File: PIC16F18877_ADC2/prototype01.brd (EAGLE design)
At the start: 95 x 72 mm, 39 parts, among them CN1 12V_IN, CN10 PIC_PORTD_IF, CN2 PIC_PORTA_IF, CN3 UART_IF, CN4 PIC_CN_H, CN5 AE-MICRO-SD-DIP, CN6 I2C_IF, CN7 PIC_PORTB_IF, CN8 PIC_PORTE_IF, CN9 PIC_PORTC_IF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

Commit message: 実体配線図の初版
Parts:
- moved R2 10.3 mm to (72.4, 31.4), turned to 0 degrees
- moved D1 8.91 mm to (82.5, 32.4), turned to 90 degrees
- moved R8 4.02 mm to (74.9, 38.1), turned to 270 degrees
- moved R7 2.86 mm to (70.8, 38.1), turned to 270 degrees
- moved C3 1.27 mm to (82.5, 39.4)
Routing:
- net SCL1: track 17.4 -> 76.8 mm
- net +12V: track 22.0 -> 71.5 mm
- net N$4: track 43.8 -> 83.6 mm, vias 0 -> 1
- net RD7: track 0.00 -> 39.7 mm, vias 0 -> 1
- net N$7: track 6.88 -> 45.8 mm
- net N$2: track 39.8 -> 77.8 mm, vias 0 -> 1
- net N$18: track 0.00 -> 37.5 mm
- net N$19: track 0.00 -> 36.2 mm
- net RD6: track 0.00 -> 34.7 mm, vias 0 -> 1
- net N$6: track 13.4 -> 46.6 mm
- net RD5: track 0.00 -> 30.3 mm, vias 0 -> 1
- net N$12: track 5.61 -> 35.0 mm
- net N$8: track 12.7 -> 41.6 mm
- net RD4: track 0.00 -> 24.7 mm
- net +3V3: track 117.8 -> 139.8 mm
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
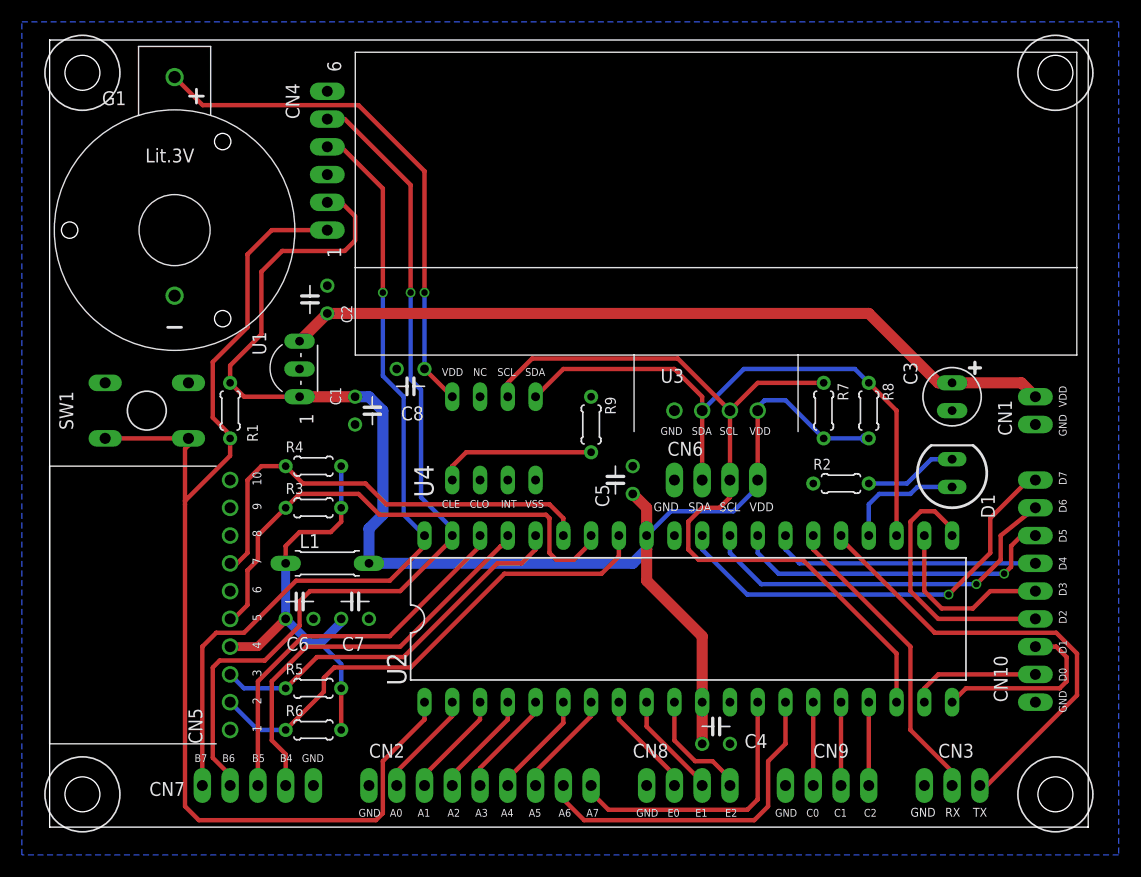
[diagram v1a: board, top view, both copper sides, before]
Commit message: 実体配線図の見直し
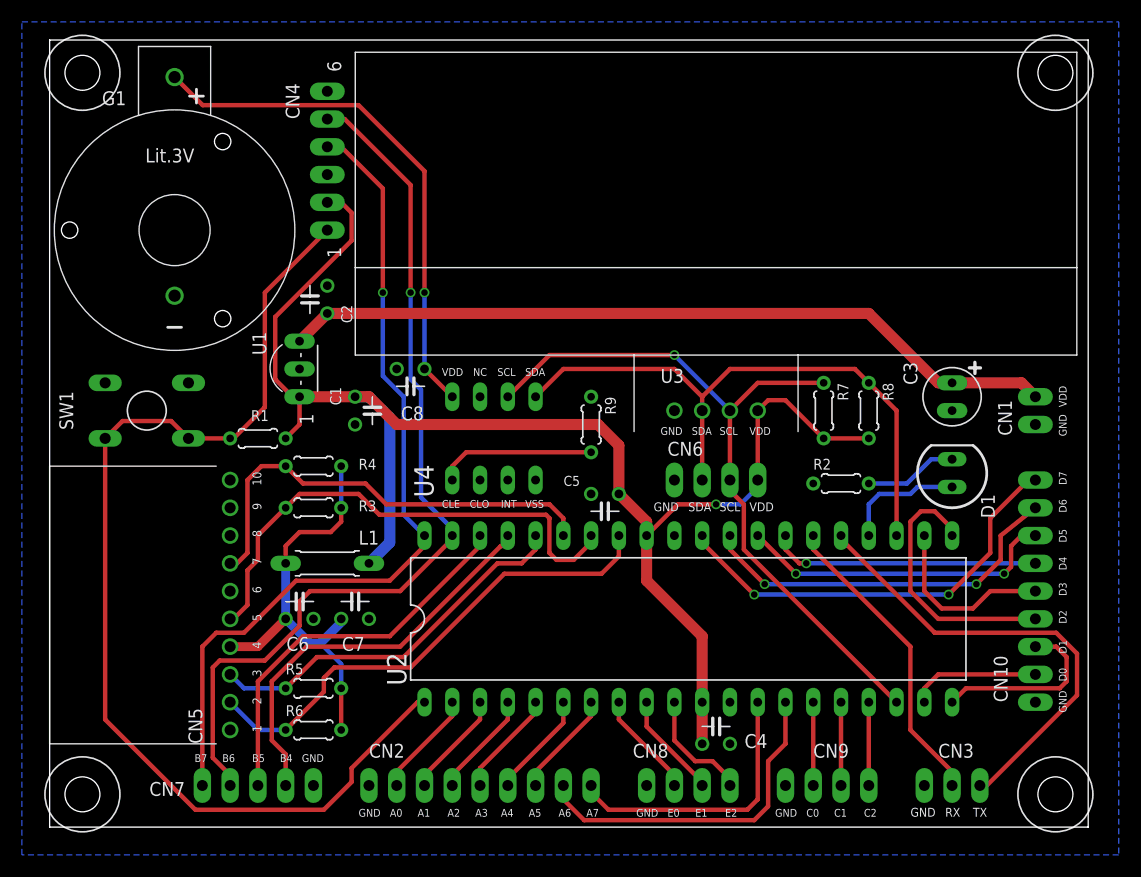
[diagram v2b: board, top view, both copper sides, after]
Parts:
- moved R1 3.59 mm to (19.1, 35.6), turned to 0 degrees
- moved C5 2.84 mm to (50.8, 30.5), turned to 180 degrees
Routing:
- net SCL1: track 76.8 -> 66.6 mm, vias 0 -> 1
- net N$3: track 106.5 -> 98.8 mm
- net RD4: track 24.7 -> 25.9 mm, vias 0 -> 1
- net +3V3: track 139.8 -> 138.6 mm, vias 0 -> 1
- net RD5: track 30.3 -> 29.4 mm, vias 1 -> 2
- net SDA1: track 57.3 -> 56.8 mm
- net RD7: track 39.7 -> 39.3 mm, vias 1 -> 2
- net RD6: track 34.7 -> 34.6 mm, vias 1 -> 2
